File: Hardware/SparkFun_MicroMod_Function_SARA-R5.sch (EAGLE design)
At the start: 83 parts, among them IC2 SN74AVC4T774PW, J1 MICROMOD_FUNCTION_STANDARD, J2 U.FL, J5 U.FL, J9 NANO_SIM, Q2 310mA/60V/1.6Ω, Q3 310mA/60V/1.6Ω, Q5 310mA/60V/1.6Ω, Q6 310mA/60V/1.6Ω, U11 74HC1G04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

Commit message: added GNSS antenna U.FL
-added GNSS antenna U.FL, with supporting circuitry and power control
-rotated module 90 degrees
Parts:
- removed C16: T520D337M006ATE045, untitled:T520D337M006ATE045
- removed C34: 33pF, New_Parts:33PF-0402-25V-5%-X7R
- removed D11, D12: PESD0402-0402T, SparkFun-DiscreteSemi:PESD0402-0402T
- removed J5: U.FL, SparkFun-Connectors:U.FL2PIN
- removed U6: LARA-R6001, HPG_Solution:LARA-R6001
- added C1: 1.0uF, SparkFun-Capacitors:1.0UF-0603-16V-10%
- added C2: 0.1uF, SparkFun-Capacitors:0.1UF-0603-25V-(+80/-20%)
- added C3: 47pF, SparkFun-Capacitors:47PF-0603-50V-5%
- added C4: 27pF, New_Parts:27PF-0402-25V-5%-X7R
- added D10, D4: PESD0402, New_Parts:PESD0402
- added FB1: 30Ω/1.8A, SparkFun-Coils:FERRITE_BEAD-0603
- added J4: U.FL, SparkFun-Connectors:U.FL2PIN
- added JP4: JUMPER-SMT_2_NC_TRACE_SILK, SparkFun-Jumpers:JUMPER-SMT_2_NC_TRACE_SILK
- added R2: 100k, SparkFun-Resistors:100KOHM-0402T-1/16W-1%
- added R23: 10k, SparkFun-Resistors:10KOHM-0603-1/10W-1%
- added R24: 10, SparkFun-Resistors:10OHM-0603-1/10W-1%
- added TP22: TEST-POINT3, SparkFun-Connectors:TEST-POINT3
- added U1: SARA-R510M8S, SparkFun-RF:SARA-R510M8S
- added U3: 3.3V, SparkFun-IC-Power:V_REG_AP2112K-3.3V
- L2: value DNP -> 68nH; device New_Parts:INDUCTOR_DNP-0402 -> New_Parts:68NH-0402
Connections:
- removed net LTE_ANT2: C34.1, L2.1, U6.ANT2
- removed net N$10: C21.+, C23.1, C25.1, D1.C, D2.C, R33.2, U8.IN
- removed net N$15: C33.2, D11.1, J2.SIGNAL
- new net ANT_REG_EN: JP4.1, R2.1, U3.EN
- new net GNSS_ANT: D4.1, FB1.2, J4.SIGNAL, U1.ANT_GNSS
- new net N$11: C33.2, J2.SIGNAL, L2.2
- new net N$18: C4.1, D10.1, L2.1, R23.2
- new net N$24: C1.1, C2.1, R24.1, U3.OUT
- new net N$25: C3.1, FB1.1, R24.2, TP22.1
- new net SARA_ANT_DET: R23.1, U1.ANT_DET
- new net VIN: C21.+, C23.1, C25.1, D1.C, D2.C, R2.2, R33.2, U3.IN, U8.IN
- net 3.3V: now also U1.VCC; no longer C16.1, U6.VCC
- net GND: now also C1.2, C2.2, C3.2, C4.2, D10.2, D4.2, J4.GND, U1.GND, U3.GND; no longer C16.2, D11.2, D12.2, J5.GND, L2.2, U6.GND
- net LTE_18_!RESET!: now also U1.RESET_N; no longer U6.RESET_N
- net LTE_18_CTS: now also U1.CTS_O; no longer U6.CTS_O
- net LTE_18_DTR: now also U1.DTR_I; no longer U6.DTR_I
- net LTE_18_NI: now also U1.GPIO1; no longer U6.GPIO1
- net LTE_18_PWR_ON: now also U1.PWR_ON; no longer U6.PWR_ON
- net LTE_18_RI: now also U1.RI_O; no longer U6.RI_O
- net LTE_18_RTS: now also U1.RTS_I; no longer U6.RTS_I
- net LTE_18_RXO: now also U1.RXD_O; no longer U6.RXD_O
- net LTE_18_TXI: now also U1.TXD_I; no longer U6.TXD_I
- net LTE_ANT: now also U1.ANT; no longer U6.ANT
- net N$4: now also J1.F4, JP4.2; no longer C34.2, D12.1, J5.SIGNAL
- net SIM_CLK: now also U1.SIM_CLK; no longer U6.SIM_CLK
- net SIM_DET: now also U1.GPIO5; no longer U6.GPIO5
- net SIM_IO: now also U1.SIM_IO; no longer U6.SIM_IO
- net SIM_RST: now also U1.SIM_RST; no longer U6.SIM_RST
- net USB_N: now also U1.USB_D-; no longer U6.USB_D-
- net USB_P: now also U1.USB_D+; no longer U6.USB_D+
- net VCCIO: now also U1.V_INT; no longer U6.V_INT
- net VSIM: now also U1.VSIM; no longer U6.VSIM
- net V_USB: now also U1.VUSB_DET; no longer U6.VUSB_DET
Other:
- note added: "AP2112K-3.3V 3.3V @ 600mA Iq = 50µA"
- note added: "GNSS Antenna"
- note added: "LTE Antenna"
- note added: "LTE Cellular Modem SARA-R5"
- note removed: "If U1 equals SARA-R510S or LENA-R8001 then L2, C34, E2, D12 : DNP"
- note removed: "If U1 equals SARA-R510S then C16, C23 : DNP"
- note removed: "LTE Antennas"
- note removed: "LTE Cellular Modem LARA-R6, LENA-R8 or SARA-R5"
- moved on the sheet: C18, C19, C20, C22, C24, C33, J2, JP3, L1, L2, R1, R11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

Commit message: top poly to 7mil and sch cleanup
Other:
- note removed: "SWAP back signals RX/TX and RTS/CTS they were swapped on the mainboard"
- moved on the sheet: C17, C23, C25, C36, C37, C38, C39, C40, D15, D16, D17, D18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

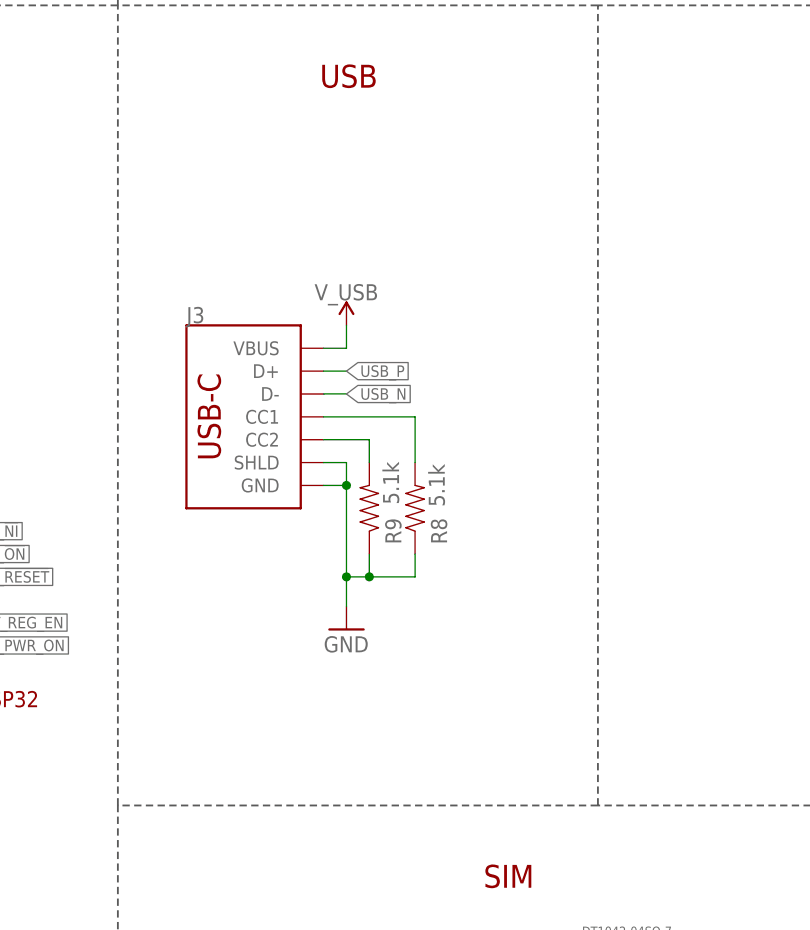
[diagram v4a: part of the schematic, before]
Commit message: USB D+ and D- routing
-re-did calcs and changed to 9 mil width with 8 mil spacing.
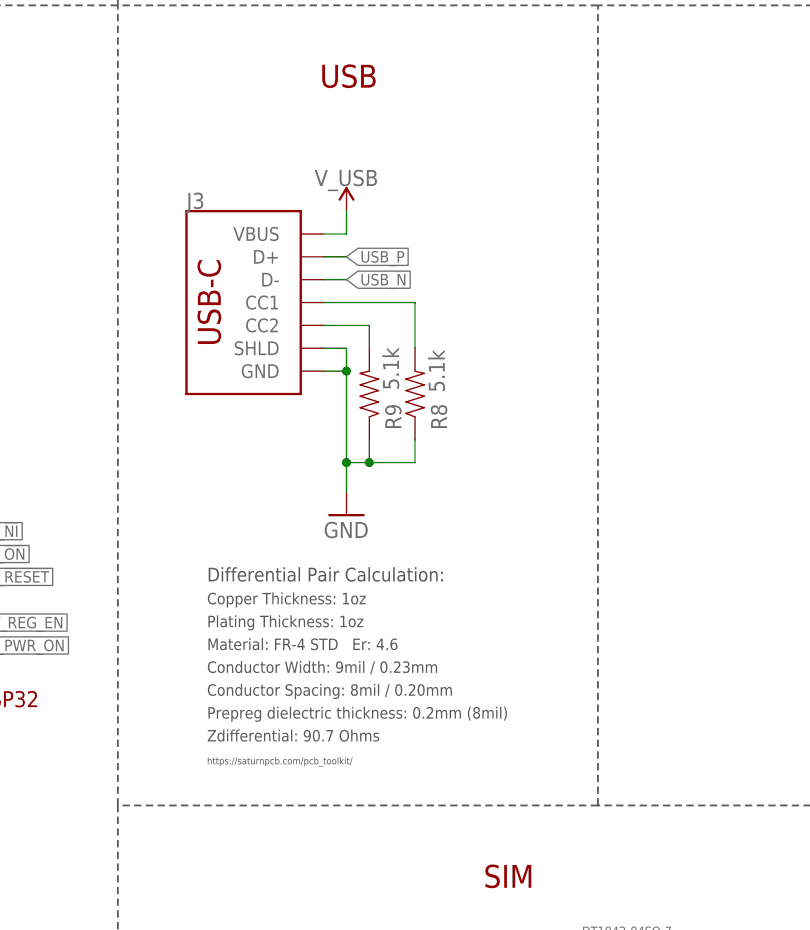
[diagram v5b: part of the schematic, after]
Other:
- note added: "Conductor Spacing: 8mil / 0.20mm"
- note added: "Conductor Width: 9mil / 0.23mm"
- note added: "Copper Thickness: 1oz"
- note added: "Differential Pair Calculation:"
- note added: "Material: FR-4 STD Er: 4.6"
- note added: "Plating Thickness: 1oz"
- note added: "Prepreg dielectric thickness: 0.2mm (8mil)"
- note added: "Zdifferential: 90.7 Ohms"
- note added: "https://saturnpcb.com/pcb_toolkit/"
- moved on the sheet: J3, R8, R9
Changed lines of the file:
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@@
 <clearance class="3" value="0.1778"/>
 </class>
-<class number="4" name="DiffPair" width="0.1524" drill="0">
-<clearance class="4" value="0.1778"/>
+<class number="4" name="DiffPair" width="0.2286" drill="0">
+<clearance class="4" value="0.2032"/>
 </class>
 </classes>
@@
 <text x="243.84" y="185.42" size="2.54" layer="97" font="vector">50Ω</text>
 <wire x1="330.2" y1="35.56" x2="330.2" y2="78.74" width="0.2032" layer="97" style="longdash"/>
+<text x="134.366" y="98.552" size="1.27" layer="97">Plating Thickness: 1oz</text>
+<text x="134.366" y="96.012" size="1.27" layer="97">Material: FR-4 STD   Er: 4.6</text>
+<text x="134.366" y="101.092" size="1.27" layer="97">Copper Thickness: 1oz</text>
+<text x="134.366" y="90.932" size="1.27" layer="97">Conductor Spacing: 8mil / 0.20mm</text>
+<text x="134.366" y="93.472" size="1.27" layer="97">Conductor Width: 9mil / 0.23mm</text>
+<text x="134.366" y="88.392" size="1.27" layer="97">Prepreg dielectric thickness: 0.2mm (8mil)</text>
+<text x="134.366" y="83.312" size="0.762" layer="97">https://saturnpcb.com/pcb_toolkit/</text>
+<text x="134.366" y="103.632" size="1.524" layer="97" ratio="15">Differential Pair Calculation:</text>
+<text x="134.366" y="85.852" size="1.27" layer="97">Zdifferential: 90.7 Ohms</text>
 </plain>
 <instances>
@@
 <attribute name="VALUE" x="111.76" y="262.382" size="1.778" layer="96" font="vector" align="bottom-center"/>
 </instance>
-<instance part="GND26" gate="1" x="149.86" y="98.298" smashed="yes">
-<attribute name="VALUE" x="147.32" y="95.758" size="1.778" layer="96" font="vector"/>
-</instance>
-<instance part="J3" gate="J1" x="134.62" y="121.92" smashed="yes">
-<attribute name="VALUE" x="132.08" y="109.474" size="1.778" layer="96" font="vector" rot="MR180" align="top-left"/>
-<attribute name="NAME" x="132.08" y="132.334" size="1.778" layer="95" font="vector"/>
-</instance>
-<instance part="R8" gate="R1" x="157.48" y="111.76" smashed="yes" rot="R90">
-<attribute name="NAME" x="161.036" y="109.22" size="1.778" layer="95" font="vector" rot="R90" align="bottom-center"/>
-<attribute name="VALUE" x="159.004" y="114.3" size="1.778" layer="96" font="vector" rot="R90" align="top-center"/>
-</instance>
-<instance part="R9" gate="R1" x="152.4" y="111.76" smashed="yes" rot="MR90">
-<attribute name="NAME" x="154.178" y="109.22" size="1.778" layer="95" font="vector" rot="MR90" align="bottom-center"/>
-<attribute name="VALUE" x="155.702" y="114.554" size="1.778" layer="96" font="vector" rot="MR90" align="top-center"/>
+<instance part="GND26" gate="1" x="149.86" y="110.998" smashed="yes">
+<attribute name="VALUE" x="147.32" y="108.458" size="1.778" layer="96" font="vector"/>
+</instance>
+<instance part="J3" gate="J1" x="134.62" y="134.62" smashed="yes">
+<attribute name="VALUE" x="132.08" y="122.174" size="1.778" layer="96" font="vector" rot="MR180" align="top-left"/>
+<attribute name="NAME" x="132.08" y="145.034" size="1.778" layer="95" font="vector"/>
+</instance>
+<instance part="R8" gate="R1" x="157.48" y="124.46" smashed="yes" rot="R90">
+<attribute name="NAME" x="161.036" y="121.92" size="1.778" layer="95" font="vector" rot="R90" align="bottom-center"/>
+<attribute name="VALUE" x="159.004" y="127" size="1.778" layer="96" font="vector" rot="R90" align="top-center"/>
+</instance>
+<instance part="R9" gate="R1" x="152.4" y="124.46" smashed="yes" rot="MR90">
+<attribute name="NAME" x="154.178" y="121.92" size="1.778" layer="95" font="vector" rot="MR90" align="bottom-center"/>
+<attribute name="VALUE" x="155.702" y="127.254" size="1.778" layer="96" font="vector" rot="MR90" align="top-center"/>
 </instance>
 <instance part="FD1" gate="G$1" x="426.72" y="33.02" smashed="yes"/>
@@
 <attribute name="VALUE" x="22.86" y="247.904" size="1.016" layer="96" font="vector" rot="MR90" align="top-left"/>
 </instance>
-<instance part="SUPPLY19" gate="G$1" x="149.86" y="132.08" smashed="yes">
-<attribute name="VALUE" x="149.86" y="134.874" size="1.778" layer="96" font="vector" align="bottom-center"/>
+<instance part="SUPPLY19" gate="G$1" x="149.86" y="144.78" smashed="yes">
+<attribute name="VALUE" x="149.86" y="147.574" size="1.778" layer="96" font="vector" align="bottom-center"/>
 </instance>
 <instance part="SUPPLY20" gate="G$1" x="10.16" y="259.08" smashed="yes">
@@
 <pinref part="GND26" gate="1" pin="GND"/>
 <pinref part="J3" gate="J1" pin="GND"/>
-<wire x1="149.86" y1="114.3" x2="149.86" y2="104.14" width="0.1524" layer="91"/>
-<wire x1="149.86" y1="104.14" x2="149.86" y2="100.838" width="0.1524" layer="91"/>
-<wire x1="147.32" y1="114.3" x2="149.86" y2="114.3" width="0.1524" layer="91"/>
-<junction x="149.86" y="104.14"/>
+<wire x1="149.86" y1="127" x2="149.86" y2="116.84" width="0.1524" layer="91"/>
+<wire x1="149.86" y1="116.84" x2="149.86" y2="113.538" width="0.1524" layer="91"/>
+<wire x1="147.32" y1="127" x2="149.86" y2="127" width="0.1524" layer="91"/>
+<junction x="149.86" y="116.84"/>
 <pinref part="R9" gate="R1" pin="1"/>
-<wire x1="152.4" y1="104.14" x2="149.86" y2="104.14" width="0.1524" layer="91"/>
-<wire x1="152.4" y1="106.68" x2="152.4" y2="104.14" width="0.1524" layer="91"/>
+<wire x1="152.4" y1="116.84" x2="149.86" y2="116.84" width="0.1524" layer="91"/>
+<wire x1="152.4" y1="119.38" x2="152.4" y2="116.84" width="0.1524" layer="91"/>
 <pinref part="J3" gate="J1" pin="SHLD"/>
-<wire x1="147.32" y1="116.84" x2="149.86" y2="116.84" width="0.1524" layer="91"/>
-<wire x1="149.86" y1="116.84" x2="149.86" y2="114.3" width="0.1524" layer="91"/>
-<junction x="149.86" y="114.3"/>
+<wire x1="147.32" y1="129.54" x2="149.86" y2="129.54" width="0.1524" layer="91"/>
+<wire x1="149.86" y1="129.54" x2="149.86" y2="127" width="0.1524" layer="91"/>
+<junction x="149.86" y="127"/>
 <pinref part="R8" gate="R1" pin="1"/>
-<wire x1="157.48" y1="106.68" x2="157.48" y2="104.14" width="0.1524" layer="91"/>
-<wire x1="152.4" y1="104.14" x2="157.48" y2="104.14" width="0.1524" layer="91"/>
-<junction x="152.4" y="104.14"/>
+<wire x1="157.48" y1="119.38" x2="157.48" y2="116.84" width="0.1524" layer="91"/>
+<wire x1="152.4" y1="116.84" x2="157.48" y2="116.84" width="0.1524" layer="91"/>
+<junction x="152.4" y="116.84"/>
 </segment>
 <segment>
@@
 <segment>
 <pinref part="J3" gate="J1" pin="CC1"/>
-<wire x1="147.32" y1="121.92" x2="157.48" y2="121.92" width="0.1524" layer="91"/>
-<wire x1="157.48" y1="121.92" x2="157.48" y2="116.84" width="0.1524" layer="91"/>
+<wire x1="147.32" y1="134.62" x2="157.48" y2="134.62" width="0.1524" layer="91"/>
+<wire x1="157.48" y1="134.62" x2="157.48" y2="129.54" width="0.1524" layer="91"/>
 <pinref part="R8" gate="R1" pin="2"/>
 </segment>
@@
 <segment>
 <pinref part="J3" gate="J1" pin="CC2"/>
-<wire x1="147.32" y1="119.38" x2="152.4" y2="119.38" width="0.1524" layer="91"/>
-<wire x1="152.4" y1="119.38" x2="152.4" y2="116.84" width="0.1524" layer="91"/>
+<wire x1="147.32" y1="132.08" x2="152.4" y2="132.08" width="0.1524" layer="91"/>
+<wire x1="152.4" y1="132.08" x2="152.4" y2="129.54" width="0.1524" layer="91"/>
 <pinref part="R9" gate="R1" pin="2"/>
 </segment>
@@
 <pinref part="J3" gate="J1" pin="VBUS"/>
 <pinref part="SUPPLY19" gate="G$1" pin="V_USB"/>
-<wire x1="147.32" y1="129.54" x2="149.86" y2="129.54" width="0.1524" layer="91"/>
-<wire x1="149.86" y1="129.54" x2="149.86" y2="132.08" width="0.1524" layer="91"/>
+<wire x1="147.32" y1="142.24" x2="149.86" y2="142.24" width="0.1524" layer="91"/>
+<wire x1="149.86" y1="142.24" x2="149.86" y2="144.78" width="0.1524" layer="91"/>
 </segment>
 <segment>
@@
 </segment>
 </net>
-<net name="USB_P" class="0">
+<net name="USB_P" class="4">
 <segment>
 <pinref part="J3" gate="J1" pin="D+"/>
-<wire x1="147.32" y1="127" x2="149.86" y2="127" width="0.1524" layer="91"/>
-<label x="149.86" y="127" size="1.27" layer="95" font="vector" xref="yes"/>
+<wire x1="147.32" y1="139.7" x2="149.86" y2="139.7" width="0.1524" layer="91"/>
+<label x="149.86" y="139.7" size="1.27" layer="95" font="vector" xref="yes"/>
 </segment>
 <segment>
@@
 </segment>
 </net>
-<net name="USB_N" class="0">
+<net name="USB_N" class="4">
 <segment>
 <pinref part="J3" gate="J1" pin="D-"/>
-<wire x1="147.32" y1="124.46" x2="149.86" y2="124.46" width="0.1524" layer="91"/>
-<label x="149.86" y="124.46" size="1.27" layer="95" font="vector" xref="yes"/>
-</segment>
-<segment>
+<wire x1="147.32" y1="137.16" x2="149.86" y2="137.16" width="0.1524" layer="91"/>
+<label x="149.86" y="137.16" size="1.27" layer="95" font="vector" xref="yes"/>
+</segment>
+<segment>

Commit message: update LEDs and limiting resistor values to new standards
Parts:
- D16, D3: device SparkFun-LED:LED-RED0603 -> SparkFun-LED:LED-RED_0603-KB
- R4: value 1k -> 4.7k; device SparkFun-Resistors:1KOHM-0402T-1/16W-1% -> SparkFun-Resistors:4.7KOHM-0402T-1/16W-1%
- R43: value 220 -> 240; device SparkFun-Resistors:220OHM-0603-1/10W-1% -> SparkFun-Resistors:240OHM-0603-1/10W-1%
- R46: value 100 -> 330; device SparkFun-Resistors:100OHM-0603-1/10W-1% -> SparkFun-Resistors:330OHM-0603-1/10W-1%
- R49: value 1k -> 2.2k; device SparkFun-Resistors:1KOHM-0402T-1/16W-1% -> SparkFun-Resistors:2.2KOHM-0402T-1/16W-1%
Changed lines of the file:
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@@
 <part name="SUPPLY55" library="SparkFun-PowerSymbols" deviceset="VCCIO" device=""/>
 <part name="SUPPLY56" library="SparkFun-PowerSymbols" deviceset="VCCIO" device=""/>
-<part name="R49" library="SparkFun-Resistors" deviceset="1KOHM" device="-0402T-1/16W-1%" value="1k"/>
-<part name="D16" library="SparkFun-LED" deviceset="LED-RED" device="0603" value="RED"/>
-<part name="R43" library="SparkFun-Resistors" library_urn="urn:adsk.eagle:library:532" deviceset="220OHM" device="-0603-1/10W-1%" package3d_urn="urn:adsk.eagle:package:39650/1" value="220"/>
+<part name="R49" library="SparkFun-Resistors" deviceset="2.2KOHM" device="-0402T-1/16W-1%" value="2.2k"/>
+<part name="D16" library="SparkFun-LED" deviceset="LED-RED" device="_0603-KB" value="RED"/>
+<part name="R43" library="SparkFun-Resistors" deviceset="240OHM" device="-0603-1/10W-1%" value="240"/>
 <part name="D17" library="SparkFun-LED" deviceset="LED-GREEN" device="0603" value="GREEN"/>
-<part name="R46" library="SparkFun-Resistors" deviceset="100OHM" device="-0603-1/10W-1%" value="100"/>
+<part name="R46" library="SparkFun-Resistors" deviceset="330OHM" device="-0603-1/10W-1%" value="330"/>
 <part name="C24" library="HPG_Solution" deviceset="8.2PF" device="-0603-50V-10%" package3d_urn="urn:adsk.eagle:package:37414/1" value="8.2pF">
 <attribute name="PROD_ID" value="CAP-16662"/>
@@
 <part name="SUPPLY10" library="SparkFun-PowerSymbols" deviceset="3.3V" device=""/>
 <part name="SUPPLY12" library="SparkFun-PowerSymbols" deviceset="3.3V" device=""/>
-<part name="R4" library="SparkFun-Resistors" deviceset="1KOHM" device="-0402T-1/16W-1%" value="1k"/>
-<part name="D3" library="SparkFun-LED" deviceset="LED-RED" device="0603" value="RED"/>
+<part name="R4" library="SparkFun-Resistors" deviceset="4.7KOHM" device="-0402T-1/16W-1%" value="4.7k"/>
+<part name="D3" library="SparkFun-LED" deviceset="LED-RED" device="_0603-KB" value="RED"/>
 <part name="J2" library="SparkFun-Connectors" deviceset="U.FL2PIN" device="" value="U.FL"/>
 <part name="J9" library="HPG_Solution_v1.0" deviceset="SIMHOLDER" device="-PUSHPUSH" value="NANO_SIM"/>
@@
 <instance part="D3" gate="G$1" x="111.76" y="254" smashed="yes">
 <attribute name="NAME" x="108.331" y="249.428" size="1.778" layer="95" font="vector" rot="R90"/>
-<attribute name="VALUE" x="113.665" y="249.428" size="1.778" layer="96" font="vector" rot="R90" align="top-left"/>
 </instance>
 <instance part="J2" gate="G$1" x="322.58" y="251.46" smashed="yes" rot="MR0">
